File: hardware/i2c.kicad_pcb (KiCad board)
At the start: 2 copper layers, 33.5 x 26.9 mm, 13 parts, among them J1 CONN_01X02, P1 USB_B, P2 CONN_01X03, P4 CONN_01X02, P5 CONN_01X09, U1 CP2112

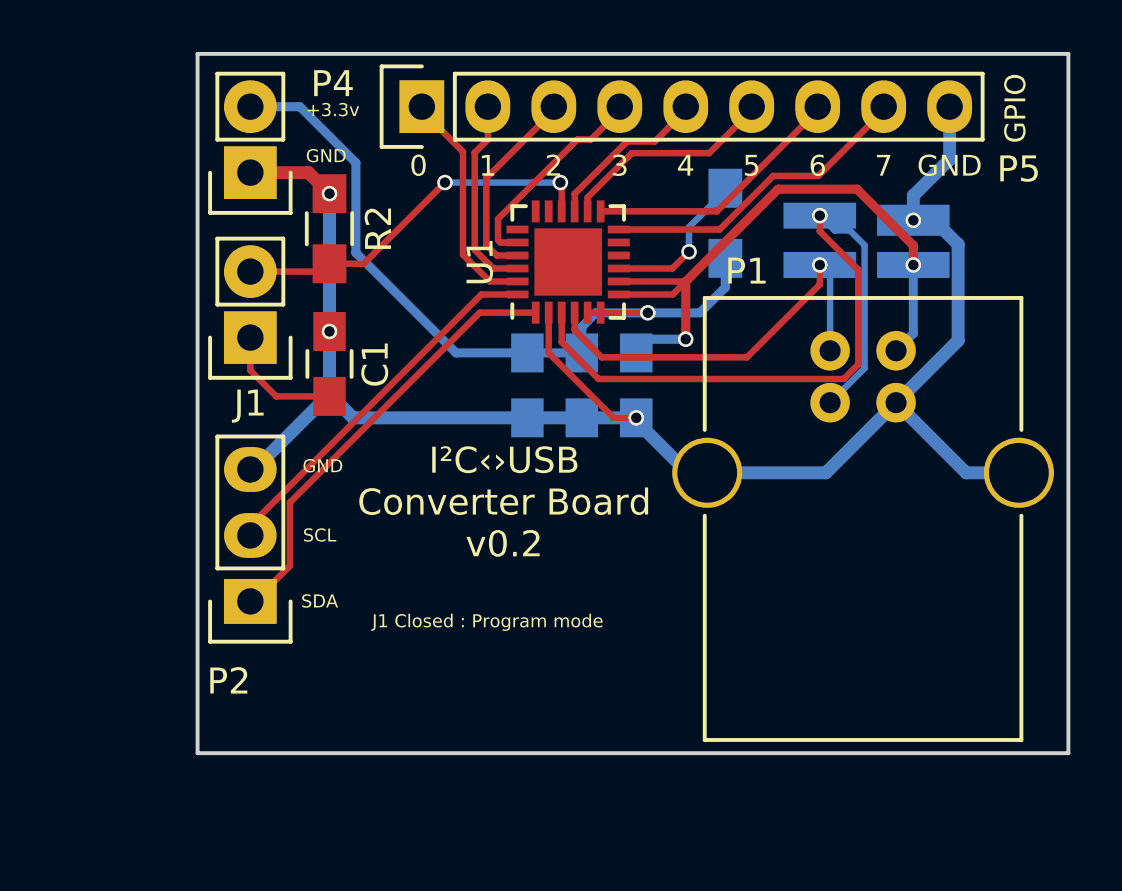
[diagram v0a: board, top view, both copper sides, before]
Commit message: New form factor.
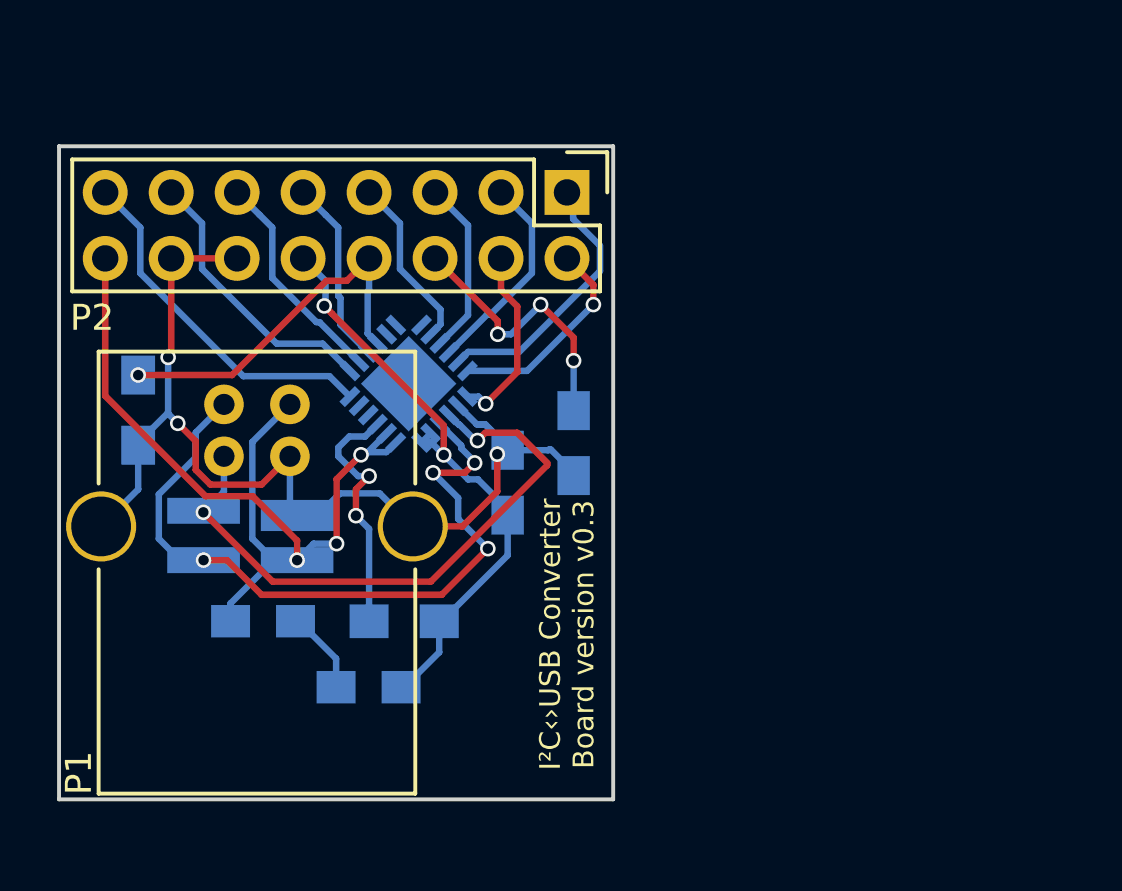
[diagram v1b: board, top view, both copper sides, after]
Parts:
- removed J1, P4: CONN_01X02, Pin_Headers:Pin_Header_Straight_1x02
- removed P5: CONN_01X09, Pin_Headers:Pin_Header_Straight_1x09
- C1, R2, U1: moved to B.Cu
- P2: value CONN_01X03 -> HEADER; footprint Pin_Headers:Pin_Header_Straight_1x03 -> Pin_Headers:Pin_Header_Straight_2x08
- moved CR1 26.3 mm to (147.8, 103.4)
- moved P1 23.4 mm to (149.4, 98.3)
- moved P2 19.9 mm to (160.0, 90.2), turned to 270 degrees
- moved R1 19.7 mm to (153.8, 106.7), turned to 180 degrees
- moved C2 17.0 mm to (148.3, 106.7), turned to 0 degrees
- moved C4 13.1 mm to (152.4, 109.2), turned to 180 degrees
- moved R2 10.2 mm to (143.5, 98.6), turned to 270 degrees
- moved C1 9.88 mm to (160.3, 99.8)
- moved U1 7.73 mm to (153.9, 97.5), turned to 135 degrees
- moved C3 4.71 mm to (157.7, 101.3), turned to 90 degrees
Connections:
- C1 pad 1: /VPP -> GND
- C1 pad 2: GND -> Net-(C1-Pad2)
- P2 pad 1: /SDA -> /GPIO.0
- P2 pad 3: GND -> /GPIO.1
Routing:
- net GND: track 65.6 -> 44.6 mm, vias 4 -> 3
- net /D-: track 15.9 -> 28.1 mm, vias 1 -> 4
- net Net-(C1-Pad2): track 0.00 -> 10.7 mm, vias 0 -> 3
- net /VCC: track 25.2 -> 35.1 mm, vias 2 -> 3
- net /SDA: track 17.0 -> 7.18 mm, vias 0 -> 1
- net /SCL: track 14.4 -> 8.11 mm, vias 0 -> 1
- net /VDD: track 29.3 -> 23.5 mm, vias 1 -> 2
- net /VPP: track 19.2 -> 14.2 mm, vias 2 -> 1
- net /D+: track 28.5 -> 23.6 mm, vias 1 -> 2
- net Net-(R1-Pad2): track 5.99 -> 9.73 mm, vias 1 -> 2
- net /GPIO.0: track 8.88 -> 10.5 mm
- net /GPIO.7: track 12.2 -> 13.7 mm
- net /GPIO.3: track 8.17 -> 6.75 mm
- net /GPIO.2: track 7.77 -> 6.79 mm
- net /GPIO.4: track 6.43 -> 7.20 mm
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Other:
- board size 33.5 x 26.9 mm -> 21.3 x 25.1 mm
- board text added: "+5v"
- board text added: "Close to program"
- board text added: "GPIOs"
- board text added: "I²C‹›USB Converter Board version v0.3"
- board text removed: "GPIO"
- board text removed: "I²C‹›USB Converter Board v0.2"
- board text removed: "J1 Closed : Program mode"

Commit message: Add I2C pullup resistors.
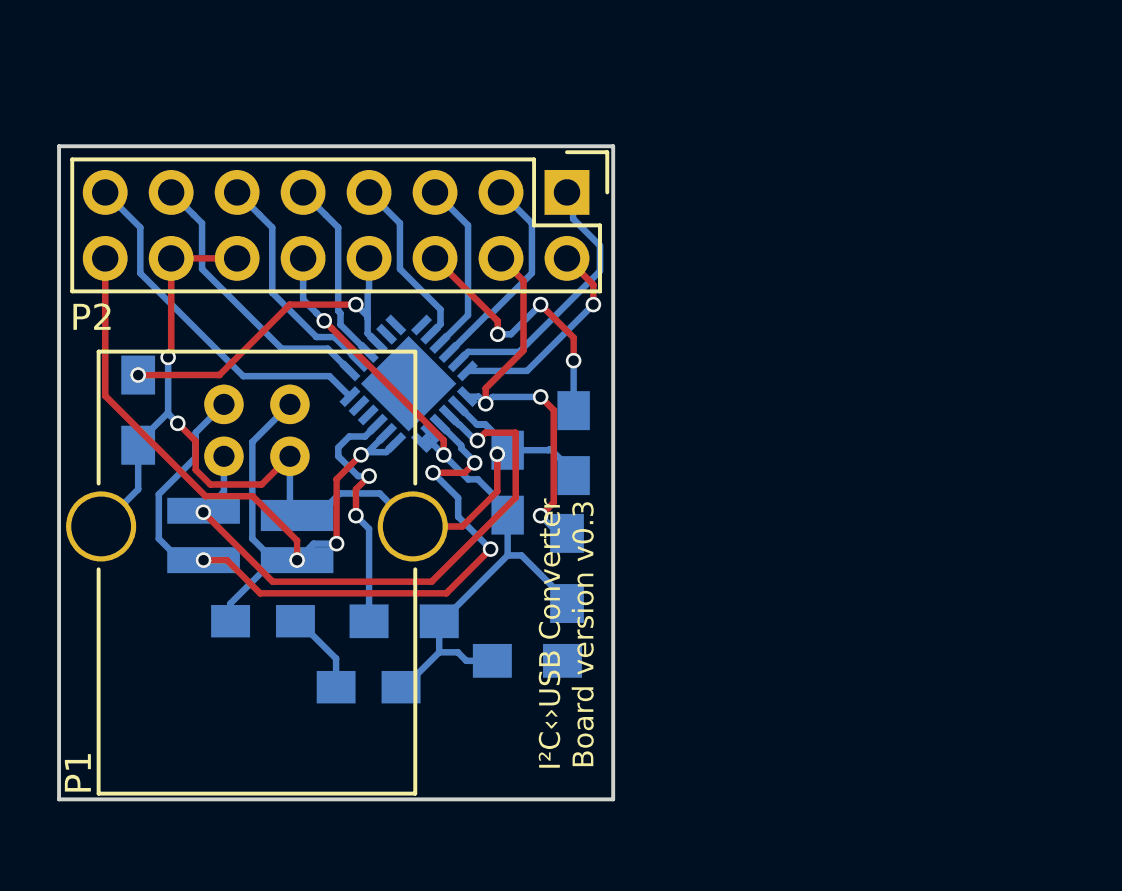
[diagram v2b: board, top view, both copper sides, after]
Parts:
- added R3: 4.7kΩ, Resistors_SMD:R_0805_HandSoldering, B.Cu at (160.0, 104.6)
- added R4: 4.7kΩ, Resistors_SMD:R_0805_HandSoldering, B.Cu at (158.5, 108.2)
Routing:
- net /SDA: track 7.18 -> 15.9 mm, vias 1 -> 3
- net /VDD: track 23.5 -> 28.8 mm
- net /D+: track 23.6 -> 22.6 mm
- net /SCL: track 8.11 -> 8.92 mm
- net /VPP: track 14.2 -> 13.7 mm, vias 1 -> 2

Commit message: Cleanup schema and layout.
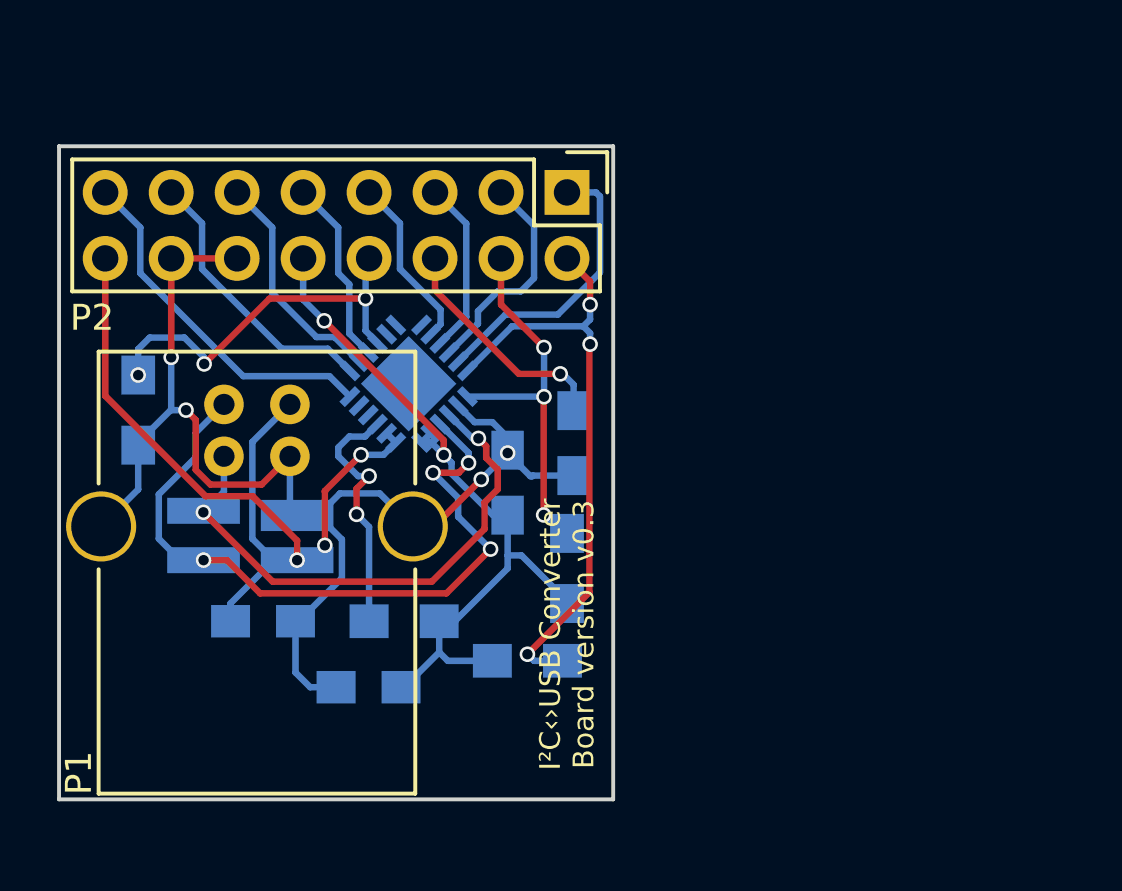
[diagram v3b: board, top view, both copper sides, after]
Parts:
- removed CR1: SP0503BAHTG, TO_SOT_Packages_SMD:SOT-143_Handsoldering
- added D1: SP0503BAHTG, TO_SOT_Packages_SMD:SOT-143_Handsoldering, B.Cu at (147.8, 103.4)
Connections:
- net /VCC renamed VCC
- net /VDD renamed VDD
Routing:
- net /SCL: track 8.92 -> 23.5 mm, vias 1 -> 3
- net GND: track 44.6 -> 48.8 mm, vias 3 -> 4
- net /D+: track 22.6 -> 20.8 mm
- net Net-(C1-Pad2): track 10.7 -> 9.06 mm, vias 3 -> 1
- net /VPP: track 13.7 -> 15.1 mm, vias 2 -> 3
- net /SDA: track 15.9 -> 14.7 mm
- net VCC: track 35.1 -> 34.0 mm
- net /GPIO.0: track 10.5 -> 11.1 mm
- net /GPIO.1: track 8.06 -> 8.57 mm
